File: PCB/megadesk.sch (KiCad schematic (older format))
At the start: 20 parts, among them J1 Interface, J2 FFC, J3 AVR-ISP-6, U1 L7812, U2 L7805, U3 ATtiny841-SS, U4 MCP2003B

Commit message: v6 gerbers
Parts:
- C1: footprint Capacitor_SMD:C_1206_3216Metric -> Capacitor_SMD:C_0805_2012Metric; LCSC C307572 -> C1740
- C3, C5: footprint Capacitor_SMD:C_1206_3216Metric -> Capacitor_SMD:C_0805_2012Metric; LCSC C24497 -> C49678
- C4: value 0.1uF -> DNP; footprint Capacitor_SMD:C_1206_3216Metric -> Capacitor_SMD:C_0805_2012Metric; LCSC C24497 -> DNP
- C6: footprint Capacitor_SMD:C_1206_3216Metric -> Capacitor_SMD:C_0603_1608Metric; LCSC C1854 -> C1603
- R1, R6: footprint Resistor_SMD:R_1206_3216Metric -> Resistor_SMD:R_0603_1608Metric; LCSC C4410 -> C21190
- R3, R4, R5: footprint Resistor_SMD:R_1206_3216Metric -> Resistor_SMD:R_0603_1608Metric; LCSC C17936 -> C23162
- U3: LCSC (none) -> DNP
- U4: LCSC C152207 -> DNP
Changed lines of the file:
@@
 F 0 "C5" H 3125 1650 50  0000 L CNN
 F 1 "0.1uF" H 3125 1450 50  0000 L CNN
-F 2 "Capacitor_SMD:C_1206_3216Metric" H 3138 1400 50  0001 C CNN
+F 2 "Capacitor_SMD:C_0805_2012Metric" H 3138 1400 50  0001 C CNN
 F 3 "" H 3100 1550 50  0001 C CNN
-F 4 "C24497" H 3100 1550 50  0001 C CNN "LCSC"
+F 4 "C49678" H 3100 1550 50  0001 C CNN "LCSC"
 F 5 "+/- 20% or better" H 3100 1550 50  0001 C CNN "Details"
 	1    3100 1550
@@
 F 0 "R5" V 6730 3050 50  0000 C CNN
 F 1 "4.7k" V 6650 3050 50  0000 C CNN
-F 2 "Resistor_SMD:R_1206_3216Metric" V 6580 3050 50  0001 C CNN
+F 2 "Resistor_SMD:R_0603_1608Metric" V 6580 3050 50  0001 C CNN
 F 3 "" H 6650 3050 50  0001 C CNN
-F 4 "C17936" H 6650 3050 50  0001 C CNN "LCSC"
+F 4 "C23162" H 6650 3050 50  0001 C CNN "LCSC"
 F 5 "+/- 10% or better" H 6650 3050 50  0001 C CNN "Details"
 	1    6650 3050
@@
 F 0 "R3" V 6730 2500 50  0000 C CNN
 F 1 "4.7k" V 6650 2500 50  0000 C CNN
-F 2 "Resistor_SMD:R_1206_3216Metric" V 6580 2500 50  0001 C CNN
+F 2 "Resistor_SMD:R_0603_1608Metric" V 6580 2500 50  0001 C CNN
 F 3 "" H 6650 2500 50  0001 C CNN
-F 4 "C17936" H 6650 2500 50  0001 C CNN "LCSC"
+F 4 "C23162" H 6650 2500 50  0001 C CNN "LCSC"
 F 5 "+/- 10% or better" H 6650 2500 50  0001 C CNN "Details"
 	1    6650 2500
@@
 F 0 "R4" V 6730 2900 50  0000 C CNN
 F 1 "4.7k" V 6650 2900 50  0000 C CNN
-F 2 "Resistor_SMD:R_1206_3216Metric" V 6580 2900 50  0001 C CNN
+F 2 "Resistor_SMD:R_0603_1608Metric" V 6580 2900 50  0001 C CNN
 F 3 "" H 6650 2900 50  0001 C CNN
-F 4 "C17936" H 6650 2900 50  0001 C CNN "LCSC"
+F 4 "C23162" H 6650 2900 50  0001 C CNN "LCSC"
 F 5 "+/- 10% or better" H 6650 2900 50  0001 C CNN "Details"
 	1    6650 2900
@@
 F 0 "C3" H 1825 1650 50  0000 L CNN
 F 1 "0.1uF" H 1825 1450 50  0000 L CNN
-F 2 "Capacitor_SMD:C_1206_3216Metric" H 1838 1400 50  0001 C CNN
+F 2 "Capacitor_SMD:C_0805_2012Metric" H 1838 1400 50  0001 C CNN
 F 3 "" H 1800 1550 50  0001 C CNN
-F 4 "C24497" H 1800 1550 50  0001 C CNN "LCSC"
+F 4 "C49678" H 1800 1550 50  0001 C CNN "LCSC"
 F 5 "+/- 20% or better" H 1800 1550 50  0001 C CNN "Details"
 	1    1800 1550
@@
 F 0 "R6" V 8680 2900 50  0000 C CNN
 F 1 "1k" V 8600 2900 50  0000 C CNN
-F 2 "Resistor_SMD:R_1206_3216Metric" V 8530 2900 50  0001 C CNN
+F 2 "Resistor_SMD:R_0603_1608Metric" V 8530 2900 50  0001 C CNN
 F 3 "" H 8600 2900 50  0001 C CNN
-F 4 "C4410" H 8600 2900 50  0001 C CNN "LCSC"
+F 4 "C21190" H 8600 2900 50  0001 C CNN "LCSC"
 F 5 "+/- 10% or better" H 8600 2900 50  0001 C CNN "Details"
 	1    8600 2900
@@
 F 0 "C6" H 8425 3300 50  0000 L CNN
 F 1 "220pF" H 8425 3100 50  0000 L CNN
-F 2 "Capacitor_SMD:C_1206_3216Metric" H 8438 3050 50  0001 C CNN
+F 2 "Capacitor_SMD:C_0603_1608Metric" H 8438 3050 50  0001 C CNN
 F 3 "" H 8400 3200 50  0001 C CNN
-F 4 "C1854" H 8400 3200 50  0001 C CNN "LCSC"
+F 4 "C1603" H 8400 3200 50  0001 C CNN "LCSC"
 F 5 "+/- 20% or better" H 8400 3200 50  0001 C CNN "Details"
 	1    8400 3200
@@
 F 0 "C1" H 850 1550 50  0000 L CNN
 F 1 "0.33uF" H 750 1450 50  0000 L CNN
-F 2 "Capacitor_SMD:C_1206_3216Metric" H 788 1400 50  0001 C CNN
+F 2 "Capacitor_SMD:C_0805_2012Metric" H 788 1400 50  0001 C CNN
 F 3 "" H 750 1550 50  0001 C CNN
-F 4 "C307572" H 750 1550 50  0001 C CNN "LCSC"
+F 4 "C1740" H 750 1550 50  0001 C CNN "LCSC"
 F 5 "+/- 20% or better" H 750 1550 50  0001 C CNN "Details"
 	1    750  1550
@@
 P 3650 2500
 F 0 "C4" H 3675 2600 50  0000 L CNN
-F 1 "0.1uF" H 3400 2400 50  0000 L CNN
-F 2 "Capacitor_SMD:C_1206_3216Metric" H 3688 2350 50  0001 C CNN
+F 1 "DNP" H 3400 2400 50  0000 L CNN
+F 2 "Capacitor_SMD:C_0805_2012Metric" H 3688 2350 50  0001 C CNN
 F 3 "" H 3650 2500 50  0001 C CNN
-F 4 "C24497" H 3650 2500 50  0001 C CNN "LCSC"
+F 4 "DNP" H 3650 2500 50  0001 C CNN "LCSC"
 F 5 "+/- 20% or better" H 3650 2500 50  0001 C CNN "Details"
 	1    3650 2500
@@
 F 0 "R1" V 5930 3750 50  0000 C CNN
 F 1 "1k" V 5850 3750 50  0000 C CNN
-F 2 "Resistor_SMD:R_1206_3216Metric" V 5780 3750 50  0001 C CNN
+F 2 "Resistor_SMD:R_0603_1608Metric" V 5780 3750 50  0001 C CNN
 F 3 "" H 5850 3750 50  0001 C CNN
-F 4 "C4410" H 5850 3750 50  0001 C CNN "LCSC"
+F 4 "C21190" H 5850 3750 50  0001 C CNN "LCSC"
 F 5 "+/- 10% or better" H 5850 3750 50  0001 C CNN "Details"
 	1    5850 3750
@@
 F 2 "Package_SO:SOIC-8_3.9x4.9mm_P1.27mm" H 7200 2500 50  0001 C CNN
 F 3 "" H 7300 2950 50  0001 C CNN
-F 4 "C152207" H 7200 2950 50  0001 C CNN "LCSC"
+F 4 "DNP" H 7200 2950 50  0001 C CNN "LCSC"
 F 5 "MCP2003B" H 7200 2950 50  0001 C CNN "Part Number"
 	1    7200 2950
@@
 F 2 "Package_SO:SOIC-14_3.9x8.7mm_P1.27mm" H 4550 3300 50  0001 C CIN
 F 3 "http://ww1.microchip.com/downloads/en/DeviceDoc/Atmel-8495-8-bit-AVR-Microcontrollers-ATtiny441-ATtiny841_Datasheet.pdf" H 4550 3300 50  0001 C CNN
+F 4 "DNP" H 4550 3300 50  0001 C CNN "LCSC"
 	1    4550 3300
 	1    0    0    -1

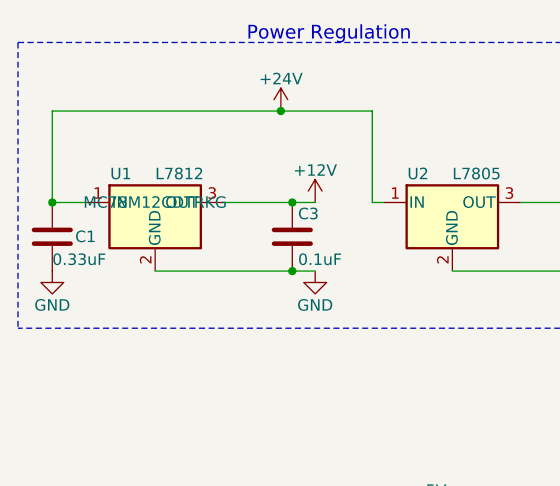
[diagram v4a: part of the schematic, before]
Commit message: Include part numbers in ibom export as per #35
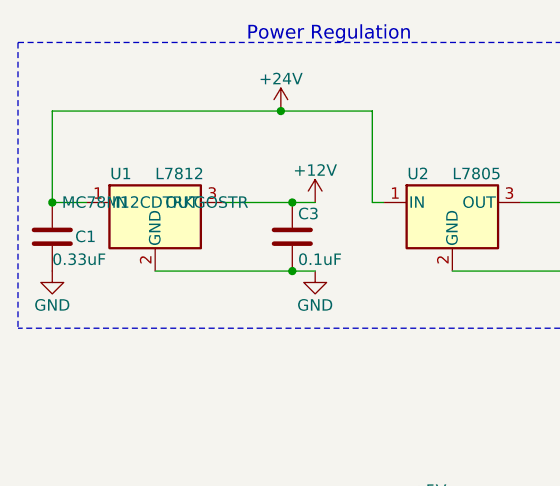
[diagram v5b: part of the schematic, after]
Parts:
- D1, D2: Part Number 1N4148 -> 1N4148WSFSCT
- J2: Part Number TE Connectivity AMP 1-84981-0 -> A100308TR-ND
- U1: Part Number MC78M12CDTRKG -> MC78M12CDTRKGOSTR
- U2: Part Number L78M05ABDT-TR -> MC78M05CDTRKGOSTR
- U3: Part Number (none) -> ATTINY841-SSURTR
- U4: Part Number MCP2003B -> MCP2003BT-E/SNTR
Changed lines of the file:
@@
 F 2 "Package_TO_SOT_SMD:TO-252-3_TabPin2" H 2525 1250 50  0001 L CIN
 F 3 "" H 2500 1350 50  0001 C CNN
-F 4 "L78M05ABDT-TR" H 2500 1400 50  0001 C CNN "Part Number"
+F 4 "MC78M05CDTRKGOSTR" H 2500 1400 50  0001 C CNN "Part Number"
 F 5 "C58069" H 2500 1400 50  0001 C CNN "LCSC"
 F 6 "35V INPUT" H 2500 1400 50  0001 C CNN "Notes"
@@
 F 2 "Package_TO_SOT_SMD:TO-252-3_TabPin2" H 1225 1250 50  0001 L CIN
 F 3 "" H 1200 1350 50  0001 C CNN
-F 4 "MC78M12CDTRKG" H 1200 1400 50  0000 C CNN "Part Number"
+F 4 "MC78M12CDTRKGOSTR" H 1200 1400 50  0000 C CNN "Part Number"
 F 5 "" H 1200 1400 60  0001 C CNN "Details"
 F 6 "C67851" H 1200 1400 50  0001 C CNN "LCSC"
@@
 F 3 "" H 7800 2500 50  0001 C CNN
 F 4 "C2128" H 7800 2500 50  0001 C CNN "LCSC"
-F 5 "1N4148" H 7800 2500 50  0001 C CNN "Part Number"
+F 5 "1N4148WSFSCT" H 7800 2500 50  0001 C CNN "Part Number"
 F 6 "Substitution OK" H 7800 2500 50  0001 C CNN "Notes"
 	1    7800 2500
@@
 F 3 "" H 8350 2750 50  0001 C CNN
 F 4 "C2128" H 8350 2750 50  0001 C CNN "LCSC"
-F 5 "1N4148" H 8350 2750 50  0001 C CNN "Part Number"
+F 5 "1N4148WSFSCT" H 8350 2750 50  0001 C CNN "Part Number"
 F 6 "Substitution OK" H 8350 2750 50  0001 C CNN "Notes"
 	1    8350 2750
@@
 F 2 "!Custom:FFC_10" H 6050 1250 50  0001 C CNN
 F 3 "" H 6050 1250 50  0001 C CNN
-F 4 "TE Connectivity AMP 1-84981-0" H 6050 1250 50  0001 C CNN "Part Number"
+F 4 "A100308TR-ND" H 6050 1250 50  0001 C CNN "Part Number"
 F 5 "DNP" H 6050 1250 50  0001 C CNN "LCSC"
 F 6 "Substitution OK" H 6050 1250 50  0001 C CNN "Notes"
@@
 F 3 "" H 7300 2950 50  0001 C CNN
 F 4 "DNP" H 7200 2950 50  0001 C CNN "LCSC"
-F 5 "MCP2003B" H 7200 2950 50  0001 C CNN "Part Number"
+F 5 "MCP2003BT-E/SNTR" H 7200 2950 50  0001 C CNN "Part Number"
 	1    7200 2950
 	1    0    0    -1
@@
 F 3 "http://ww1.microchip.com/downloads/en/DeviceDoc/Atmel-8495-8-bit-AVR-Microcontrollers-ATtiny441-ATtiny841_Datasheet.pdf" H 4550 3300 50  0001 C CNN
 F 4 "DNP" H 4550 3300 50  0001 C CNN "LCSC"
+F 5 "ATTINY841-SSURTR" H 4550 3300 50  0001 C CNN "Part Number"
 	1    4550 3300
 	1    0    0    -1
